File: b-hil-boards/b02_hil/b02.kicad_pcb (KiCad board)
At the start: 2 copper layers, 100 x 50 mm, 22 parts, among them J2 Conn_01x06_Socket, K1 Relay_DPDT, K2 Relay_DPDT, K3 Relay_DPDT, K4 Relay_DPDT, U1 MAX485E, U2 ULN2003, U3 ADuM1412, U4 ESP32_C3_SuperMini, U5 OLED-128x64-I2C

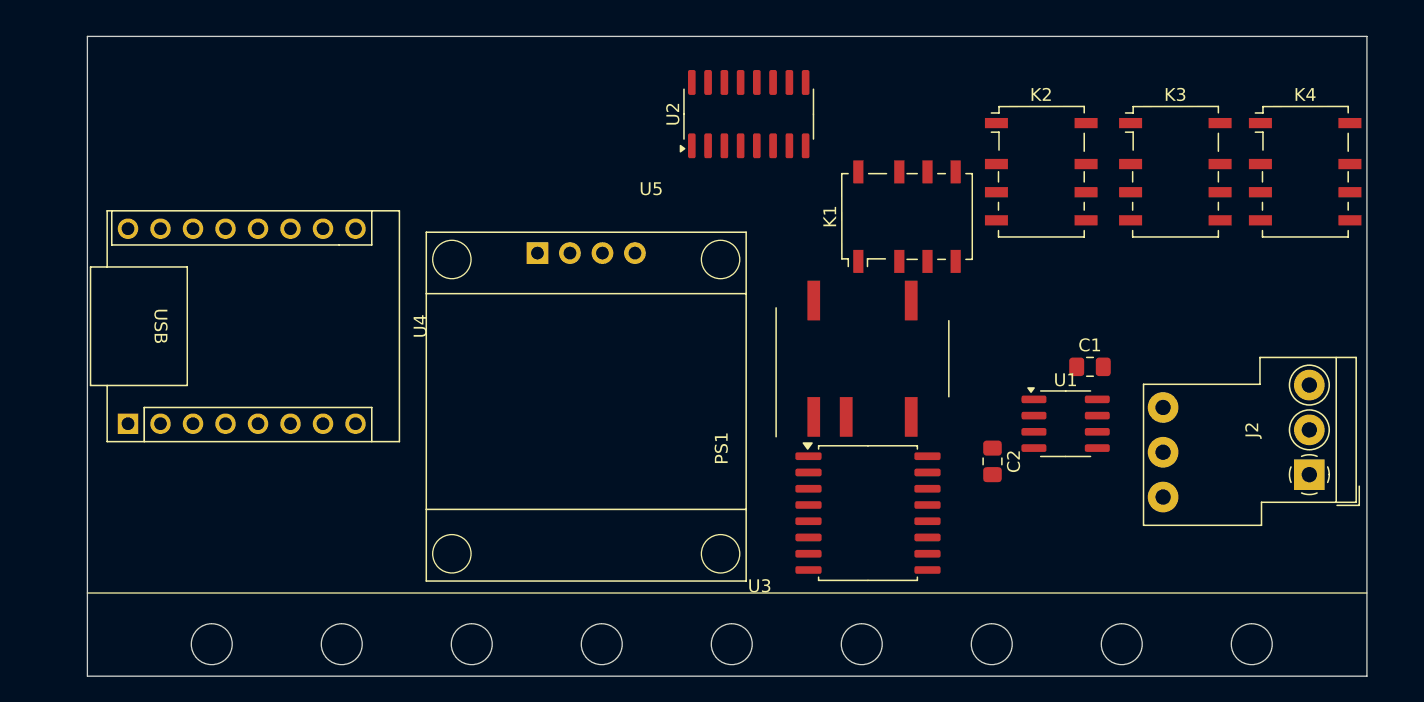
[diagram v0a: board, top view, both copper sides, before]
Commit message: B02 card: routing and silkscreen completed
- PCB layout and silkscreen finished for b02_hil
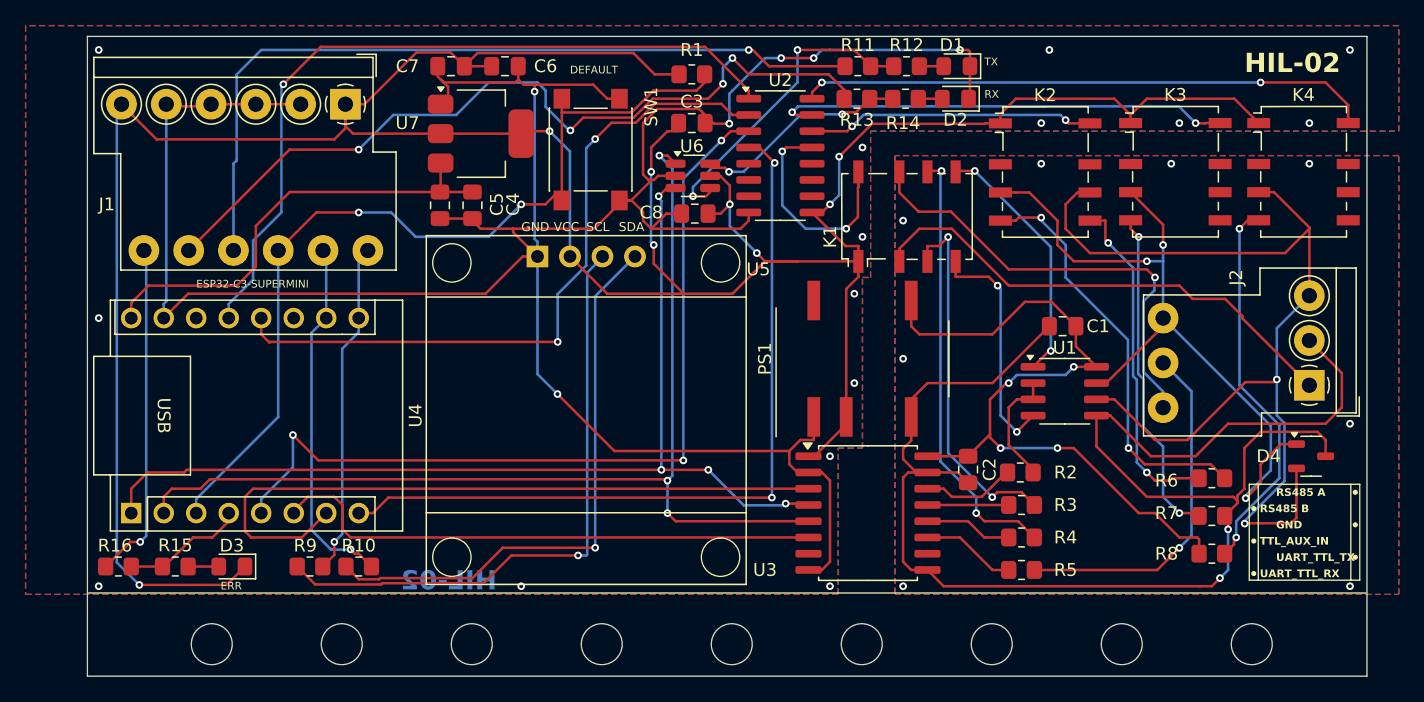
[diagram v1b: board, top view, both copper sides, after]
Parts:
- added C3: C, Capacitor_SMD:C_0805_2012Metric_Pad1.18x1.45mm_HandSolder, F.Cu at (127.0, 41.3)
- added C4: C, Capacitor_SMD:C_0805_2012Metric_Pad1.18x1.45mm_HandSolder, F.Cu at (109.9, 47.7)
- added C5: C, Capacitor_SMD:C_0805_2012Metric_Pad1.18x1.45mm_HandSolder, F.Cu at (107.3, 47.7)
- added C6: C, Capacitor_SMD:C_0805_2012Metric_Pad1.18x1.45mm_HandSolder, F.Cu at (112.4, 36.8)
- added C7: C, Capacitor_SMD:C_0805_2012Metric_Pad1.18x1.45mm_HandSolder, F.Cu at (108.2, 36.8)
- added C8: C, Capacitor_SMD:C_0805_2012Metric_Pad1.18x1.45mm_HandSolder, F.Cu at (127.2, 48.4)
- added D1: LED, LED_SMD:LED_0805_2012Metric_Pad1.15x1.40mm_HandSolder, F.Cu at (147.7, 36.8)
- added D2: LED, LED_SMD:LED_0805_2012Metric_Pad1.15x1.40mm_HandSolder, F.Cu at (147.6, 39.4)
- added D3: LED, LED_SMD:LED_0805_2012Metric_Pad1.15x1.40mm_HandSolder, F.Cu at (91.0, 75.9)
- added D4: D_TVS_Dual_AAC, Package_TO_SOT_SMD:SOT-23-3, F.Cu at (175.4, 67.3)
- added J1: Conn_01x12_Socket, TerminalBlock_DoubleLevel:TerminalBlock_DoubleLevel_2x06_P3.50mm_Horizontal, F.Cu at (99.9, 39.8)
- added R1: R, Resistor_SMD:R_0805_2012Metric_Pad1.20x1.40mm_HandSolder, F.Cu at (127.0, 37.5)
- added R10: R, Resistor_SMD:R_0805_2012Metric_Pad1.20x1.40mm_HandSolder, F.Cu at (101.0, 75.9)
- added R11: R, Resistor_SMD:R_0805_2012Metric_Pad1.20x1.40mm_HandSolder, F.Cu at (140.0, 36.8)
- added R12: R, Resistor_SMD:R_0805_2012Metric_Pad1.20x1.40mm_HandSolder, F.Cu at (143.8, 36.8)
- added R13: R, Resistor_SMD:R_0805_2012Metric_Pad1.20x1.40mm_HandSolder, F.Cu at (139.9, 39.4)
- added R14: R, Resistor_SMD:R_0805_2012Metric_Pad1.20x1.40mm_HandSolder, F.Cu at (143.7, 39.4)
- added R15: R, Resistor_SMD:R_0805_2012Metric_Pad1.20x1.40mm_HandSolder, F.Cu at (86.6, 75.9)
- added R16: R, Resistor_SMD:R_0805_2012Metric_Pad1.20x1.40mm_HandSolder, F.Cu at (82.2, 75.9)
- added R2: R, Resistor_SMD:R_0805_2012Metric_Pad1.20x1.40mm_HandSolder, F.Cu at (152.7, 68.6)
- added R3: R, Resistor_SMD:R_0805_2012Metric_Pad1.20x1.40mm_HandSolder, F.Cu at (152.8, 71.1)
- added R4: R, Resistor_SMD:R_0805_2012Metric_Pad1.20x1.40mm_HandSolder, F.Cu at (152.8, 73.7)
- added R5: R, Resistor_SMD:R_0805_2012Metric_Pad1.20x1.40mm_HandSolder, F.Cu at (152.8, 76.2)
- added R6: R, Resistor_SMD:R_0805_2012Metric_Pad1.20x1.40mm_HandSolder, F.Cu at (167.6, 69.0)
- added R7: R, Resistor_SMD:R_0805_2012Metric_Pad1.20x1.40mm_HandSolder, F.Cu at (167.6, 72.0)
- added R8: R, Resistor_SMD:R_0805_2012Metric_Pad1.20x1.40mm_HandSolder, F.Cu at (167.6, 74.9)
- added R9: R, Resistor_SMD:R_0805_2012Metric_Pad1.20x1.40mm_HandSolder, F.Cu at (97.2, 75.9)
- added SW1: SW_Push, Button_Switch_SMD:SW_Push_1P1T_NO_6x6mm_H9.5mm, F.Cu at (119.1, 43.3)
- added U6: 74LVC2G34, Package_TO_SOT_SMD:SOT-23-6_Handsoldering, F.Cu at (127.1, 45.4)
- added U7: AMS1117-3.3, Package_TO_SOT_SMD:SOT-223-3_TabPin2, F.Cu at (110.5, 42.1)
- moved U4 6.99 mm to (83.2, 71.8)
- moved J2 6.98 mm to (175.3, 61.8)
- moved U2 4.08 mm to (133.9, 43.8), turned to 0 degrees
- moved C1 3.83 mm to (156.0, 57.1), turned to 180 degrees
- moved U1 2.54 mm to (156.1, 62.2)
- moved C2 2.01 mm to (148.6, 68.3)
- moved K2 0.31 mm to (154.6, 45.1)
- moved U5 0.27 mm to (114.9, 51.7)
- moved K4 0.13 mm to (174.8, 45.1)
- renumbered REF** to MH01, REF** to MH02, REF** to MH03, REF** to MH04, REF** to MH05, REF** to MH06, REF** to MH07, REF** to MH08, REF** to MH09
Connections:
- C1 pad 1: +3V3 -> +3.3V
- C2 pad 1: +3V3 -> +3.3V
- J2 pad 1: unconnected-(J2-Pin_1-Pad1) -> /UART1_TTL_TX
- J2 pad 2: unconnected-(J2-Pin_2-Pad2) -> /UART1_TTL_RX
- J2 pad 4: unconnected-(J2-Pin_4-Pad4) -> /TTL_AUX_IN
- J2 pad 5: unconnected-(J2-Pin_5-Pad5) -> /R_PU
- J2 pad 6: unconnected-(J2-Pin_6-Pad6) -> /R_PD
- PS1 pad 1: unconnected-(PS1-GND-Pad1) -> GND1
- PS1 pad 2: unconnected-(PS1-Vin-Pad2) -> +3V3
- PS1 pad 5: +3V3 -> +3.3V
- U1 pad 1: unconnected-(U1-RO-Pad1) -> /UART1_485_RX
- U1 pad 4: unconnected-(U1-DI-Pad4) -> /UART1_485_TX
- U1 pad 6: unconnected-(U1-A-Pad6) -> /R_PU
- U1 pad 7: unconnected-(U1-B-Pad7) -> /R_PD
- U1 pad 8: +3V3 -> +3.3V
- U2 pad 1: unconnected-(U2-I1-Pad1) -> Net-(U2-I1)
- U2 pad 13: unconnected-(U2-O4-Pad13) -> Net-(U2-O4)
- U2 pad 14: unconnected-(U2-O3-Pad14) -> Net-(U2-O3)
- U2 pad 15: unconnected-(U2-O2-Pad15) -> Net-(U2-O2)
- U2 pad 16: unconnected-(U2-O1-Pad16) -> Net-(U2-O1)
- U2 pad 2: unconnected-(U2-I2-Pad2) -> Net-(U2-I2)
- U2 pad 3: unconnected-(U2-I3-Pad3) -> Net-(U2-I3)
- U2 pad 4: unconnected-(U2-I4-Pad4) -> Net-(U2-I4)
- U2 pad 8: unconnected-(U2-GND-Pad8) -> GND1
- U2 pad 9: unconnected-(U2-COM-Pad9) -> +3V3
- U3 pad 1: unconnected-(U3-VDD1-Pad1) -> +3V3
- U3 pad 11: unconnected-(U3-VID-Pad11) -> Net-(U3-VID)
- U3 pad 12: unconnected-(U3-VIC-Pad12) -> Net-(U3-VIC)
- U3 pad 13: unconnected-(U3-VOB-Pad13) -> Net-(U3-VOB)
- U3 pad 14: unconnected-(U3-VOA-Pad14) -> Net-(U3-VOA)
- U3 pad 16: +3V3 -> +3.3V
- U3 pad 2: unconnected-(U3-GND1-Pad2) -> GND1
- U3 pad 3: unconnected-(U3-VIA-Pad3) -> /485_CTR
- U3 pad 4: unconnected-(U3-VIB-Pad4) -> /TX
- U3 pad 5: unconnected-(U3-VOC-Pad5) -> /RX
- U3 pad 6: unconnected-(U3-VOD-Pad6) -> /TTL_IN
- U3 pad 8: unconnected-(U3-GND1-Pad8) -> GND1
- U4 pad 1: unconnected-(U4-GPIO5-Pad1) -> /TX
- U4 pad 10: unconnected-(U4-GPIO1-Pad10) -> /DISP_SDA
- U4 pad 12: unconnected-(U4-GPIO3-Pad12) -> Net-(U2-I2)
- U4 pad 13: unconnected-(U4-GPIO4-Pad13) -> Net-(U2-I1)
- U4 pad 15: unconnected-(U4-GND-Pad15) -> GND1
- U4 pad 16: unconnected-(U4-5V-Pad16) -> +5V
- U4 pad 2: unconnected-(U4-GPIO6-Pad2) -> /RX
- U4 pad 3: unconnected-(U4-GPIO7-Pad3) -> /DEFAULTS
- U4 pad 4: unconnected-(U4-GPIO8-Pad4) -> /ERR_LED
- U4 pad 5: unconnected-(U4-GPIO9-Pad5) -> Net-(U2-I3)
- U4 pad 6: unconnected-(U4-GPIO10-Pad6) -> /TTL_IN
- U4 pad 7: unconnected-(U4-GPIO20-Pad7) -> /485_CTR
- U4 pad 8: unconnected-(U4-GPIO21-Pad8) -> Net-(U2-I4)
- U4 pad 9: unconnected-(U4-GPIO0-Pad9) -> /DISP_SCL
- U5 pad 1: unconnected-(U5-GND-Pad1) -> GND1
- U5 pad 2: unconnected-(U5-VDD-Pad2) -> +3V3
- U5 pad 3: unconnected-(U5-SCL-Pad3) -> Net-(U5-SCL)
- U5 pad 4: unconnected-(U5-SDA-Pad4) -> Net-(U5-SDA)
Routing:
- net +3V3: track 0.00 -> 247.7 mm, vias 0 -> 8
- net GND1: track 0.00 -> 217.6 mm, vias 0 -> 21
- net GND2: track 0.00 -> 121.5 mm, vias 0 -> 10
- net /RX: track 0.00 -> 82.6 mm, vias 0 -> 3
- net /R_PU: track 0.00 -> 81.2 mm, vias 0 -> 2
- net /TX: track 0.00 -> 79.5 mm, vias 0 -> 4
- net /DEFAULTS: track 0.00 -> 69.9 mm, vias 0 -> 2
- net Net-(U2-I3): track 0.00 -> 67.1 mm, vias 0 -> 3
- net /RX_LED_EXT: track 0.00 -> 63.8 mm, vias 0 -> 4
- net /TX_LED_EXT: track 0.00 -> 63.2 mm, vias 0 -> 1
- net Net-(U2-I4): track 0.00 -> 61.6 mm, vias 0 -> 2
- net /R_PD: track 0.00 -> 60.2 mm, vias 0 -> 3
- net Net-(U2-I1): track 0.00 -> 59.7 mm, vias 0 -> 1
- net +3.3V: track 0.00 -> 59.5 mm, vias 0 -> 4
- net Net-(U2-I2): track 0.00 -> 55.3 mm, vias 0 -> 2
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- added copper zone on B.Cu, net GND1
- added copper zone on F.Cu, net GND1
- added copper zone on B.Cu, net GND2
- added copper zone on F.Cu, net GND2
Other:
- board text added: "DEFAULT"
- board text added: "DEFAULT_SW"
- board text added: "DISP_SCL"
- board text added: "DISP_SDA"
- board text added: "ERR"
- board text added: "ERR_LED_EXT"
- board text added: "ESP32-C3-SUPERMINI"
- board text added: "GND"
- board text added: "HIL-02"
- board text added: "RS485 A"
- board text added: "RS485 B"
- board text added: "RX"
- board text added: "RX_LED_EXT"
- board text added: "SCL"
- board text added: "SDA"
- board text added: "TTL_AUX_IN"
- board text added: "TX"
- board text added: "TX_LED_EXT"
- board text added: "UART_TTL_RX"
- board text added: "UART_TTL_TX"
- board text added: "VCC"
